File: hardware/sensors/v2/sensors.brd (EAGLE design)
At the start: 93.9 x 54.6 mm, 38 parts, among them IC1 MEGA8-AI, IC3 7805TV, IC4 MAX232ECWE

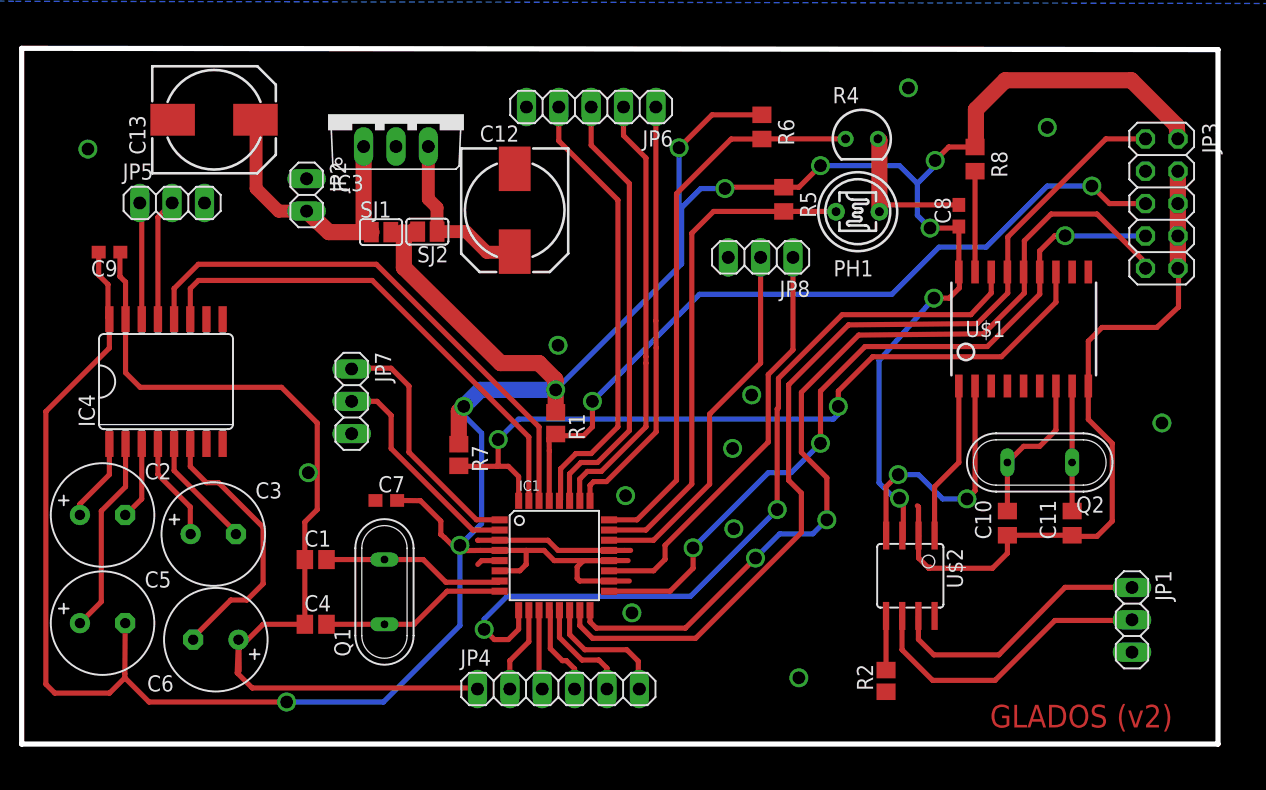
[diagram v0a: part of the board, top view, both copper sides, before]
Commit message: changes to fix a bug in the hardware and make it DRC proof
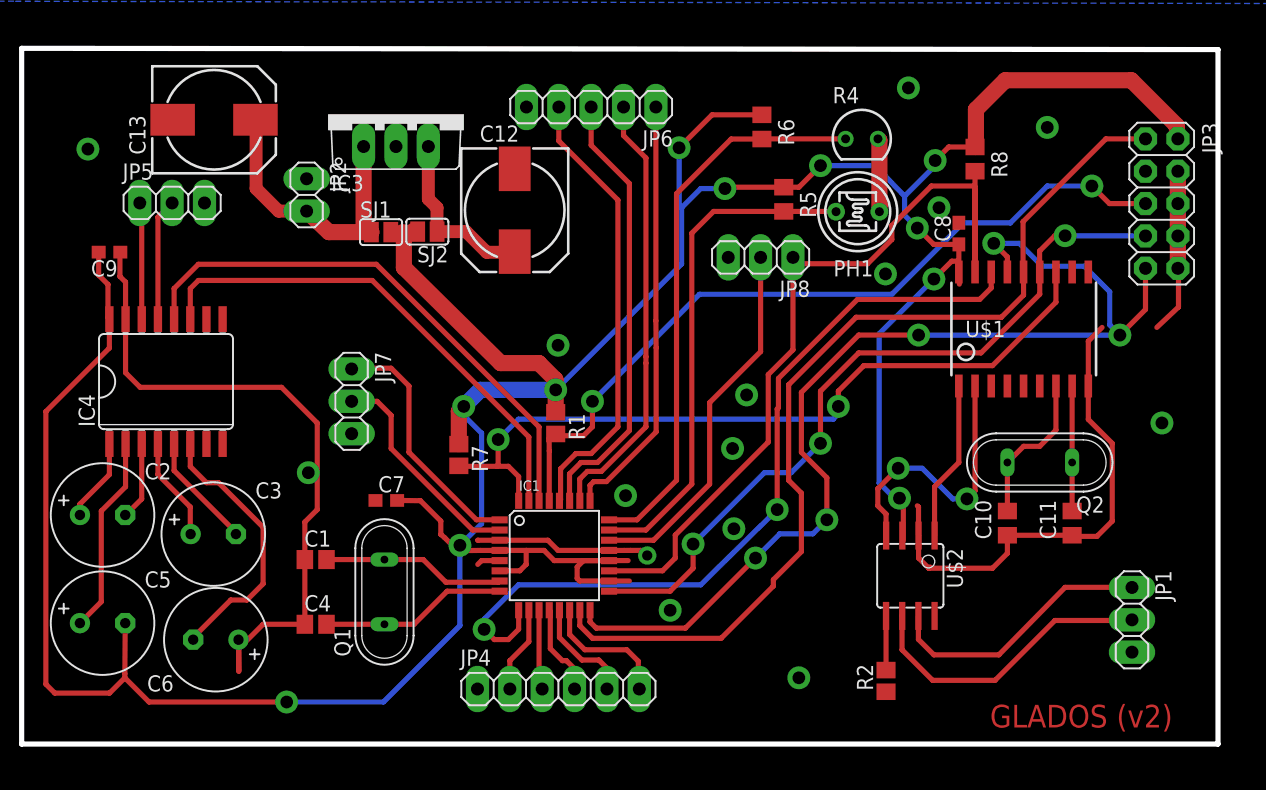
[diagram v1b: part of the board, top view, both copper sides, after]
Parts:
- moved C8 1.40 mm to (73.7, 43.4)
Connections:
- removed net N$21: R8.2, U$1.17
- removed net N$29: IC1.19, JP8.1
- new net /CANRST: IC1.19, JP8.1, R8.2, U$1.17
- net MISO: now also U$1.15; no longer U$1.14
- net MOSI: now also U$1.14; no longer U$1.15
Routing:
- net /CANRST: track 0.00 -> 65.3 mm
- net N$29: track 32.6 -> 0.00 mm
- net GND: track 157.1 -> 126.5 mm, vias 12 -> 15
- net MISO: track 71.9 -> 84.1 mm, vias 2 -> 5
- net N$21: track 7.91 -> 0.00 mm
- net VCC: track 277.2 -> 279.4 mm
- net MOSI: track 73.0 -> 75.1 mm
- net N$2: track 20.5 -> 21.7 mm
